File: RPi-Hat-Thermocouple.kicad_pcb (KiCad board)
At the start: 2 copper layers, 65 x 56 mm, 32 parts, among them J1 RPi_GPIO, J2 Push Terminal, J3 Push Terminal, J4 Push Terminal, SW1 Write, U1 AT24CS32, U2 MAX31855, U3 MAX31855, U4 MAX31855, U5 74LVC139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

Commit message: Added Alert Buzzer.
Rev 1.1 will be released soon.
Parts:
- added BZ1: Buzzer, cui-ml:CMI-9655S-SMT, F.Cu at (71.0, 42.5)
- added C10: 0.1uF, Capacitors_SMD:C_0603, F.Cu at (33.5, 74.0)
- added P1: CONN_01X03, Pin_Headers:Pin_Header_Straight_1x03_Pitch2.00mm, F.Cu at (31.5, 76.0)
- added P2: CONN_01X03, Pin_Headers:Pin_Header_Straight_1x03_Pitch2.54mm, F.Cu at (45.8, 38.1)
- added Q1: NUD3124, TO_SOT_Packages_SMD:SOT-23, F.Cu at (71.0, 50.5)
- added REF***: OSHW-Logo_11.4x12mm_SilkScreen, Symbols:OSHW-Logo_11.4x12mm_SilkScreen, B.Cu at (80.0, 56.5)
- added REF***: OSHW-Logo2_7.3x6mm_SilkScreen, Symbols:OSHW-Logo2_7.3x6mm_SilkScreen, F.Cu at (76.5, 82.5)
- BT1: value Battery_Cell -> CR1225
- moved R4 8.01 mm to (37.0, 70.0), turned to 90 degrees
- moved SW1 6.05 mm to (86.4, 48.5), turned to 0 degrees
- moved U6 5.90 mm to (37.0, 75.2), turned to 90 degrees
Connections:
- net Net-(J1-Pad24) renamed /TC_CE
- J1 pad 10: Net-(J1-Pad10) -> /RX
- J1 pad 2: Net-(J1-Pad2) -> +5V
- J1 pad 29: Net-(J1-Pad29) -> /ALERT
- J1 pad 4: Net-(J1-Pad4) -> +5V
- J1 pad 8: Net-(J1-Pad8) -> /TX
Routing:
- net +5V: track 0.00 -> 68.4 mm, vias 0 -> 1
- net /ALERT: track 0.00 -> 18.8 mm, vias 0 -> 1
- net /RX: track 0.00 -> 8.46 mm
- net /TX: track 0.00 -> 8.45 mm
- net /T_OW: track 56.8 -> 50.0 mm
- net +3V3: track 47.9 -> 51.5 mm
- net Net-(BZ1-Pad2): track 0.00 -> 3.00 mm
- net Net-(R1-Pad2): track 7.04 -> 9.62 mm
- net GND: track 14.3 -> 16.6 mm
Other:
- net class Default: via_drill 0.4 -> 0.3302
- board text added: "1-Wire"
- board text added: "Console"
- board text added: "DQ"
- board text added: "GND"
- board text added: "RX"
- board text added: "Rev 1.1 Mar 2017"
- board text added: "TX"
- board text added: "VDD"
- board text removed: "Rev 1.0 Feb 2017"

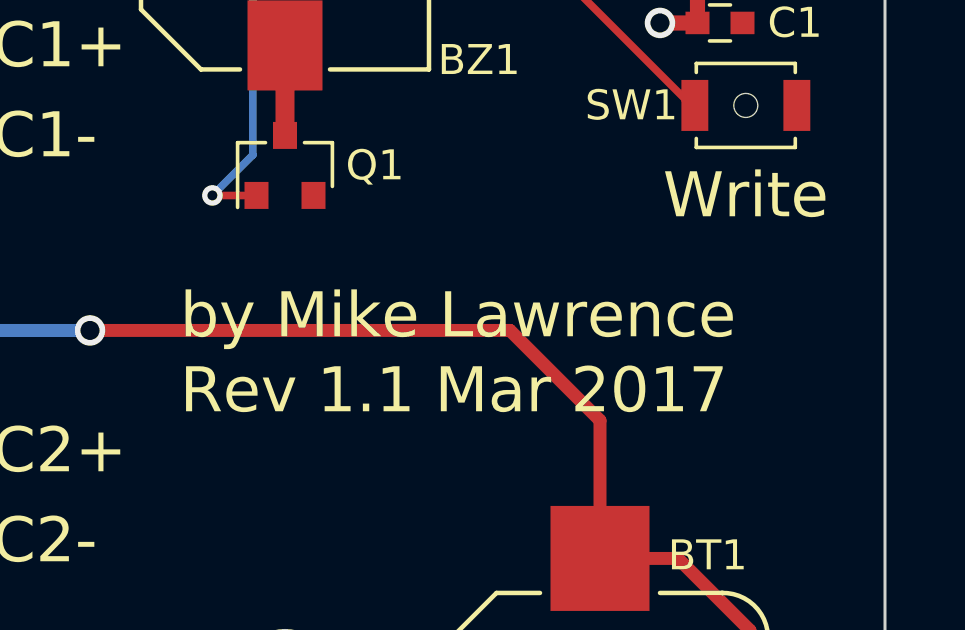
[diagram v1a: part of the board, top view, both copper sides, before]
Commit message: Add R7
R7 prevents alert from going off until software
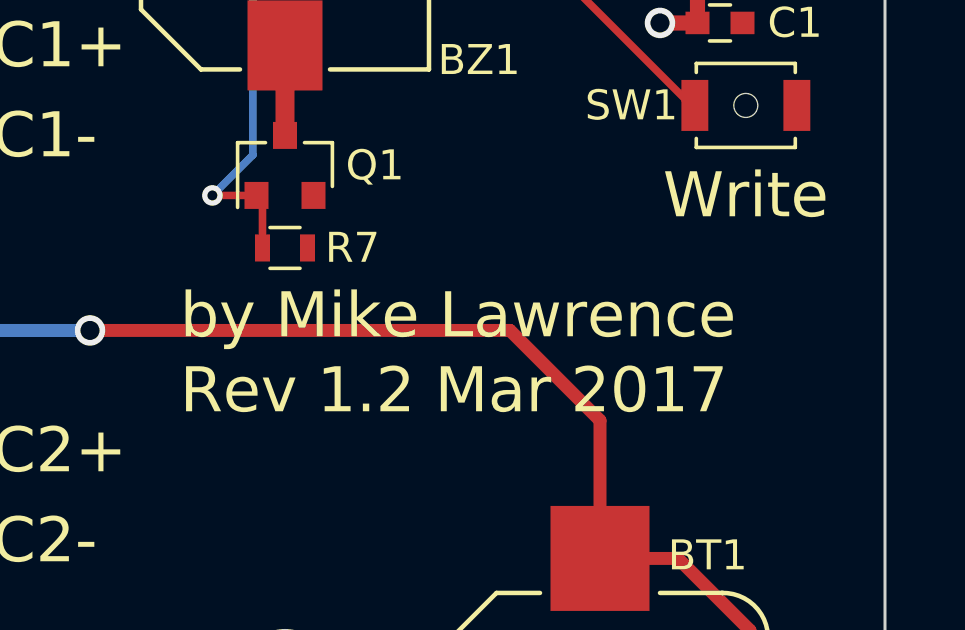
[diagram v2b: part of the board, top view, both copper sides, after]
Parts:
- added R7: 4.7k, Resistors_SMD:R_0603, F.Cu at (71.0, 53.2)
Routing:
- net /ALERT: track 18.8 -> 20.6 mm
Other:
- board text added: "Rev 1.2 Mar 2017"
- board text removed: "Rev 1.1 Mar 2017"
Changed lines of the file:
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@@
 (kicad_pcb (version 4) (host pcbnew 4.0.5)
   (general
-    (links 99)
+    (links 101)
     (no_connects 0)
     (area 25.949999 23.825 100.072954 87.12658)
     (thickness 1.6)
     (drawings 44)
-    (tracks 270)
+    (tracks 272)
     (zones 0)
-    (modules 39)
+    (modules 40)
     (nets 52)
   )
@@
     (34 B.Paste user hide)
     (35 F.Paste user hide)
-    (36 B.SilkS user hide)
+    (36 B.SilkS user)
     (37 F.SilkS user)
     (38 B.Mask user hide)
@@
       (xy -0.113933 -2.757629) (xy -0.013056 -2.757714) (xy 0 -2.757714) (xy 0.10391 -2.757652)) (layer F.SilkS) (width 0.01))
   )
-  (gr_text "Rev 1.1 Mar 2017\n" (at 69.1 60.695) (layer B.SilkS)
+  (module Resistors_SMD:R_0603 (layer F.Cu)
+    (at 71 53.25 180)
+    (descr "Resistor SMD 0603, reflow soldering, Vishay (see dcrcw.pdf)")
+    (tags "resistor 0603")
+    (attr smd)
+    (fp_text reference R7 (at -2.25 0 180) (layer F.SilkS)
+      (effects (font (size 1 1) (thickness 0.15)))
+    )
+    (fp_text value 4.7k (at 0 1.5 180) (layer F.Fab) hide
+      (effects (font (size 1 1) (thickness 0.15)))
+    )
+    (fp_text user %R (at 0 -1.45 180) (layer F.Fab) hide
+      (effects (font (size 1 1) (thickness 0.15)))
+    )
+    (fp_line (start -0.8 0.4) (end -0.8 -0.4) (layer F.Fab) (width 0.1))
+    (fp_line (start 0.8 0.4) (end -0.8 0.4) (layer F.Fab) (width 0.1))
+    (fp_line (start 0.8 -0.4) (end 0.8 0.4) (layer F.Fab) (width 0.1))
+    (fp_line (start -0.8 -0.4) (end 0.8 -0.4) (layer F.Fab) (width 0.1))
+    (fp_line (start 0.5 0.68) (end -0.5 0.68) (layer F.SilkS) (width 0.12))
+    (fp_line (start -0.5 -0.68) (end 0.5 -0.68) (layer F.SilkS) (width 0.12))
+    (fp_line (start -1.25 -0.7) (end 1.25 -0.7) (layer F.CrtYd) (width 0.05))
+    (fp_line (start -1.25 -0.7) (end -1.25 0.7) (layer F.CrtYd) (width 0.05))
+    (fp_line (start 1.25 0.7) (end 1.25 -0.7) (layer F.CrtYd) (width 0.05))
+    (fp_line (start 1.25 0.7) (end -1.25 0.7) (layer F.CrtYd) (width 0.05))
+    (pad 1 smd rect (at -0.75 0 180) (size 0.5 0.9) (layers F.Cu F.Paste F.Mask)
+      (net 2 GND))
+    (pad 2 smd rect (at 0.75 0 180) (size 0.5 0.9) (layers F.Cu F.Paste F.Mask)
+      (net 48 /ALERT))
+    (model Resistors_SMD.3dshapes/R_0603.wrl
+      (at (xyz 0 0 0))
+      (scale (xyz 1 1 1))
+      (rotate (xyz 0 0 0))
+    )
+  )
+  (gr_text "Rev 1.2 Mar 2017\n" (at 69.1 60.695) (layer B.SilkS)
     (effects (font (size 1.5 1.5) (thickness 0.3)) (justify left mirror))
   )
@@
     (effects (font (size 1.5 1.5) (thickness 0.25)))
   )
-  (gr_text "Rev 1.1 Mar 2017\n" (at 67.5 58) (layer F.SilkS)
+  (gr_text "Rev 1.2 Mar 2017\n" (at 67.5 58) (layer F.SilkS)
     (effects (font (size 1.5 1.5) (thickness 0.3)) (justify left))
   )
@@
   (via (at 73.74 38.5) (size 1.016) (drill 0.635) (layers F.Cu B.Cu) (net 46))
   (segment (start 71 49.5) (end 71 46.5) (width 0.635) (layer F.Cu) (net 47))
+  (segment (start 70.25 53.25) (end 70.25 51.7) (width 0.254) (layer F.Cu) (net 48))
+  (segment (start 70.25 51.7) (end 70.05 51.5) (width 0.254) (layer F.Cu) (net 48))
   (segment (start 69.93 34.77) (end 69.93 50.15) (width 0.254) (layer B.Cu) (net 48))
   (segment (start 69.93 50.15) (end 68.58 51.5) (width 0.254) (layer B.Cu) (net 48))

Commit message: Added Analog Power LDO regulator
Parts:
- added C11: 2.2uF, Capacitors_SMD:C_0805, F.Cu at (58.2, 39.0)
- added C12: 2.2uF, Capacitors_SMD:C_0805, F.Cu at (65.2, 39.0)
- added C13: 10nF, Capacitors_SMD:C_0603, F.Cu at (44.0, 43.2)
- added C14: 10nF, Capacitors_SMD:C_0603, F.Cu at (44.0, 56.8)
- added C15: 10nF, Capacitors_SMD:C_0603, F.Cu at (44.0, 70.2)
- added U8: MCP1754ST, TO_SOT_Packages_SMD:SOT89-3_Housing, F.Cu at (61.8, 39.6)
- moved REF*** 2.14 mm to (82.0, 57.2)
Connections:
- C10 pad 2: +3V3 -> +3.3VA
- C2 pad 1: +3V3 -> +3.3VA
- C3 pad 1: +3V3 -> +3.3VA
- C4 pad 1: +3V3 -> +3.3VA
- P1 pad 3: +3V3 -> +3.3VA
- R4 pad 1: +3V3 -> +3.3VA
- U2 pad 4: +3V3 -> +3.3VA
- U3 pad 4: +3V3 -> +3.3VA
- U4 pad 4: +3V3 -> +3.3VA
- U6 pad 3: +3V3 -> +3.3VA
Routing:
- net +3.3VA: track 0.00 -> 84.6 mm, vias 0 -> 4
- net GND: track 16.6 -> 48.9 mm
- net +3V3: track 51.5 -> 22.9 mm, vias 8 -> 5
- net +5V: track 68.4 -> 76.4 mm
- net /TC_CLK: track 62.9 -> 60.5 mm, vias 5 -> 4
- net Net-(BT1-Pad1): track 76.1 -> 74.8 mm
- net /TC_MISO: track 66.7 -> 65.6 mm, vias 5 -> 4
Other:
- board text added: "Rev 1.2 Apr 2017"
- board text removed: "Rev 1.2 Mar 2017"
